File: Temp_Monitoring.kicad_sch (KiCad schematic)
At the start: 1 part

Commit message: sch update done
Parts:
- added C151: 0.1uF, Capacitor_SMD:C_0402_1005Metric, symbol Device:C
- added C152, C153, C154, C155, C156, C157: 2.2nF, Capacitor_SMD:C_0402_1005Metric, symbol Device:C
- added R84, R85, R86, R87: 4.7k, Resistor_SMD:R_0402_1005Metric, symbol Device:R_US
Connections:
- net TEMP_P1: now reaches U20.1 (DXP1)
- net TEMP_P1: now also C152.1
- net TEMP_N5: now reaches U20.10 (DXN5)
- net TEMP_N5: now also C156.2
- net TEMP_N6: now reaches U20.11 (DXN6)
- net TEMP_N6: now also C157.2
- net TEMP_P6: now reaches U20.12 (DXP6)
- net TEMP_P6: now also C157.1
- net 3V3: now reaches U20.13 (STBY)
- net 3V3: now also U20.16 (VCC), C151.1, R84.2, R85.2, R86.2, R87.2
- net GND: now reaches U20.14 (N.C.)
- net GND: now also U20.20 (GND), C151.2
- net OVERT_TEMP: now reaches U20.15 (OVERT)
- net OVERT_TEMP: now also R87.1
- net ALERT_TEMP: now reaches U20.17 (ALERT)
- net ALERT_TEMP: now also R86.1
- net SDA: now reaches U20.18 (SDA)
- net SDA: now also R85.1
- net SCL: now reaches U20.19 (SCL)
- net SCL: now also R84.1
- net TEMP_N1: now reaches U20.2 (DXN1)
- net TEMP_N1: now also C152.2
- net TEMP_P2: now reaches U20.3 (DXP2)
- net TEMP_P2: now also C153.1
- net TEMP_N2: now reaches U20.4 (DXN2)
- net TEMP_N2: now also C153.2
- net TEMP_P3: now reaches U20.5 (DXP3)
- net TEMP_P3: now also C154.1
- net TEMP_N3: now reaches U20.6 (DXN3)
- net TEMP_N3: now also C154.2
- net TEMP_P4: now reaches U20.7 (DXP4)
- net TEMP_P4: now also C155.1
- net TEMP_N4: now reaches U20.8 (DXN4)
- net TEMP_N4: now also C155.2
- net TEMP_P5: now reaches U20.9 (DXP5)
- net TEMP_P5: now also C156.1

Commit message: Finish routing
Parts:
- U20: footprint (none) -> bitaxe:MAX6689UP9A+
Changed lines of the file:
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@@
 			)
 		)
-		(property "Footprint" ""
+		(property "Footprint" "bitaxe:MAX6689UP9A+"
 			(at 166.37 113.03 0)
 			(effects
@@
 			)
 		)
-		(property "Datasheet" ""
+		(property "Datasheet" "https://www.analog.com/media/en/technical-documentation/data-sheets/MAX6689.pdf"
 			(at 166.37 113.03 0)
 			(effects

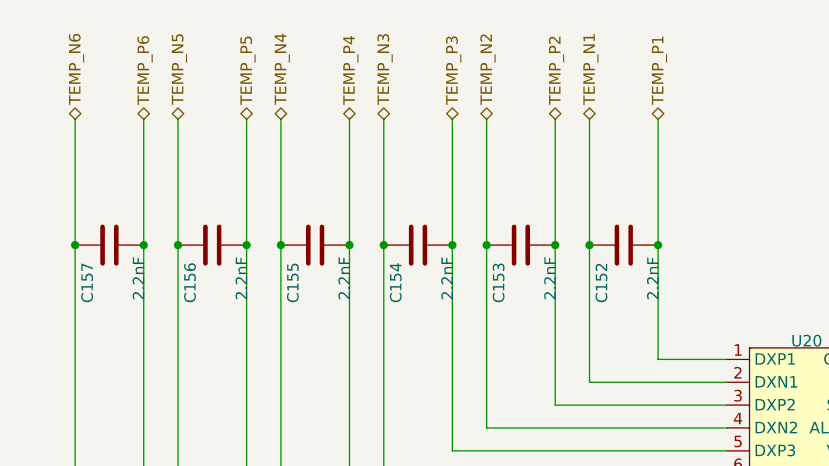
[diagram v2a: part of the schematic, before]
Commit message: Add resisters for MAX6689
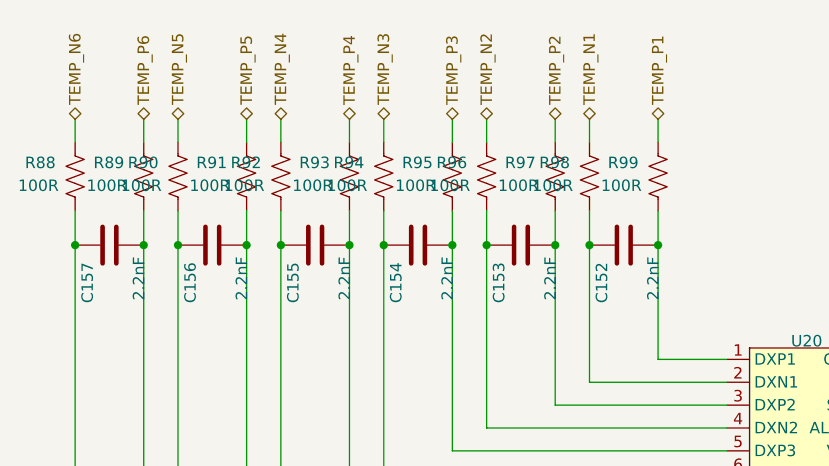
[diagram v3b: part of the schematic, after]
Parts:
- added R88, R89, R90, R91, R92, R93, R94, R95, R96, R97, R98, R99: 100R, Resistor_SMD:R_0201_0603Metric, symbol Device:R_US
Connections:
- net TEMP_N1: now also R98.1; no longer C152.2, U20.2 (DXN1)
- net TEMP_N2: now also R96.1; no longer C153.2, U20.4 (DXN2)
- net TEMP_N3: now also R94.1; no longer C154.2, U20.6 (DXN3)
- net TEMP_N4: now also R92.1; no longer C155.2, U20.8 (DXN4)
- net TEMP_N5: now also R90.1; no longer C156.2, U20.10 (DXN5)
- net TEMP_N6: now also R88.1; no longer C157.2, U20.11 (DXN6)
- net TEMP_P1: now also R99.1; no longer C152.1, U20.1 (DXP1)
- net TEMP_P2: now also R97.1; no longer C153.1, U20.3 (DXP2)
- net TEMP_P3: now also R95.1; no longer C154.1, U20.5 (DXP3)
- net TEMP_P4: now also R93.1; no longer C155.1, U20.7 (DXP4)
- net TEMP_P5: now also R91.1; no longer C156.1, U20.9 (DXP5)
- net TEMP_P6: now also R89.1; no longer C157.1, U20.12 (DXP6)
- new net: C156.1, R91.2, U20.9 (DXP5)
- new net: C156.2, R90.2, U20.10 (DXN5)
- new net: C155.1, R93.2, U20.7 (DXP4)
- new net: C155.2, R92.2, U20.8 (DXN4)
- new net: C153.1, R97.2, U20.3 (DXP2)
- new net: C153.2, R96.2, U20.4 (DXN2)
- new net: C152.1, R99.2, U20.1 (DXP1)
- new net: C152.2, R98.2, U20.2 (DXN1)
- new net: C157.2, R88.2, U20.11 (DXN6)
- new net: C154.1, R95.2, U20.5 (DXP3)
- new net: C154.2, R94.2, U20.6 (DXN3)
- new net: C157.1, R89.2, U20.12 (DXP6)
